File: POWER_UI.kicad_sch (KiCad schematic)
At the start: 45 parts, among them J601 PWR_IN1, J602 PWR_IN2, J603 PWR_IN3, J604 PWR_IN4, J605 MCP_INT, J606 5V, J607 GND, J608 3V3, J609 EX_PA, J610 EX_PB, J611 PWR_OUT1, J612 PWR_OUT3, J613 PWR_OUT2, J614 PWR_OUT4, Q601 IRLML9301TRPBF, Q602 IRLML9301TRPBF, Q603 IRLML9301TRPBF, Q604 IRLML9301TRPBF, U601 TLP291-4, U602 TLP291-4, U603 MCP23017_SS

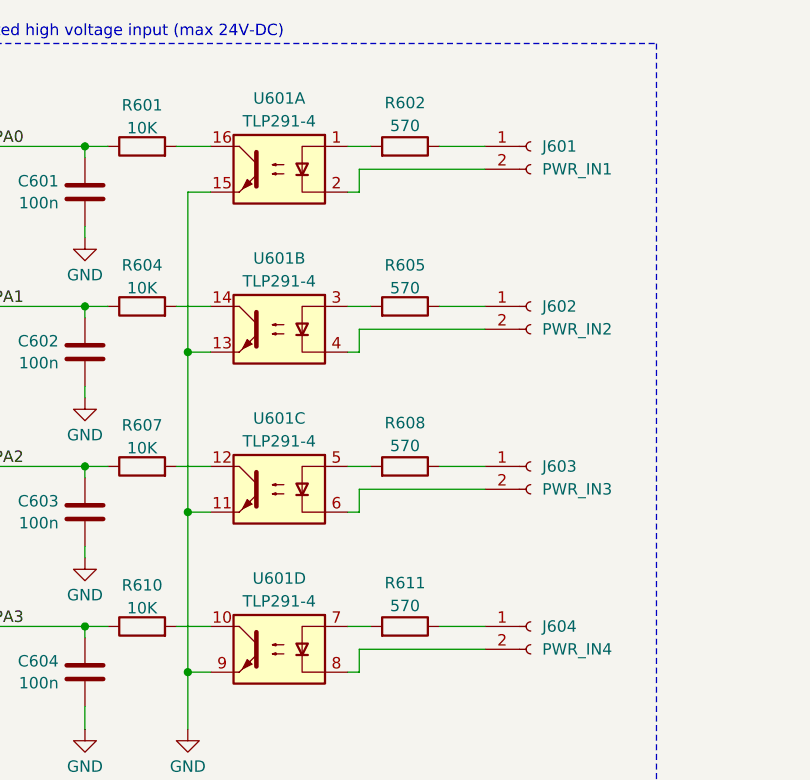
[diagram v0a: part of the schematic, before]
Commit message: added some lcsc PN, and uniformed some resistors values to reduce BOM count
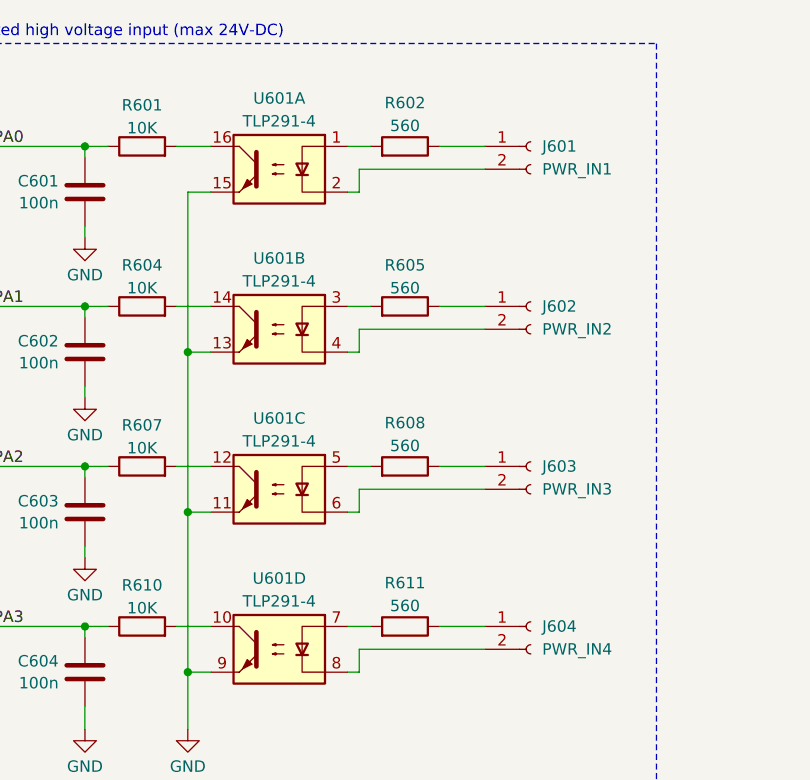
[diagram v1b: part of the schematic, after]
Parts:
- R602, R605, R608, R611: value 570 -> 560; LCSC (none) -> C23204
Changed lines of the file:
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@@
 			)
 		)
-		(property "Value" "570"
+		(property "Value" "560"
 			(at 165.1 30.734 90)
 			(effects
@@
 		)
 		(property "Sim.Type" ""
+			(at 165.1 33.02 90)
+			(effects
+				(font
+					(size 1.27 1.27)
+				)
+				(hide yes)
+			)
+		)
+		(property "LCSC" "C23204"
 			(at 165.1 33.02 90)
 			(effects
@@
 			)
 		)
-		(property "Value" "570"
+		(property "Value" "560"
 			(at 165.1 84.074 90)
 			(effects
@@
 		)
 		(property "Sim.Type" ""
+			(at 165.1 86.36 90)
+			(effects
+				(font
+					(size 1.27 1.27)
+				)
+				(hide yes)
+			)
+		)
+		(property "LCSC" "C23204"
 			(at 165.1 86.36 90)
 			(effects
@@
 			)
 		)
-		(property "Value" "570"
+		(property "Value" "560"
 			(at 165.1 66.294 90)
 			(effects
@@
 		)
 		(property "Sim.Type" ""
+			(at 165.1 68.58 90)
+			(effects
+				(font
+					(size 1.27 1.27)
+				)
+				(hide yes)
+			)
+		)
+		(property "LCSC" "C23204"
 			(at 165.1 68.58 90)
 			(effects
@@
 			)
 		)
-		(property "Value" "570"
+		(property "Value" "560"
 			(at 165.1 48.768 90)
 			(effects
@@
 			(at 165.1 50.8 90)
 			(effects
+				(font
+					(size 1.27 1.27)
+				)
+				(hide yes)
+			)
+		)
+		(property "LCSC" "C23204"
+			(at 165.1 50.8 90)
+			(effects

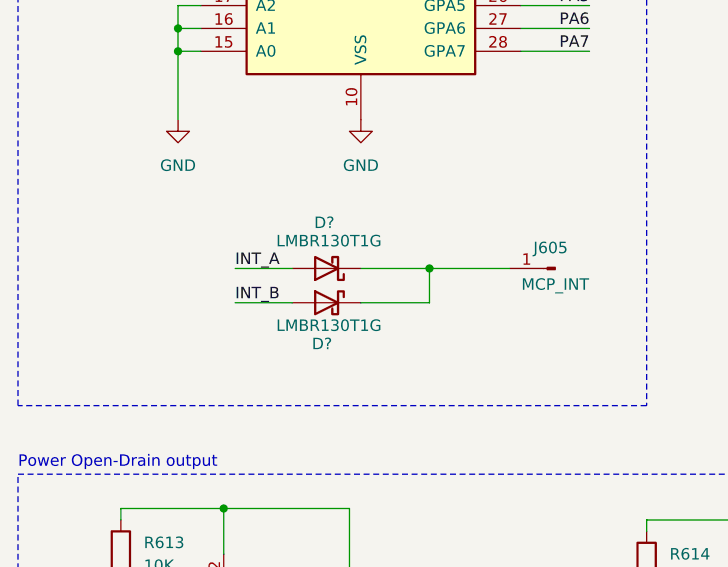
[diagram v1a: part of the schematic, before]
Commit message: Created buzzer footprint, and fixed some libraries simbols and footprint
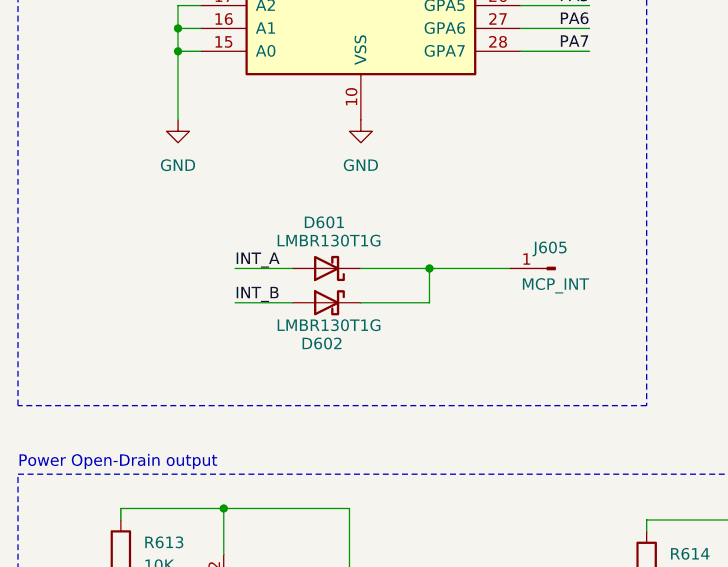
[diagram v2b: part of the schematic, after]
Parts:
- gave numbers to parts that had none: 2
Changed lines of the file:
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@@
 		(on_board yes)
 		(dnp no)
-		(property "Reference" "D?"
+		(property "Reference" "D602"
 			(at 59.182 109.982 0)
 			(effects
@@
 			(project "Educational-Board_MainBoard"
 				(path "/835b4df9-7d62-45f4-81d2-5a64fbc86f3c/ba7e13a3-22c7-43a3-af0e-4fb3e1cec0f6"
-					(reference "D?")
+					(reference "D602")
 					(unit 1)
 				)
@@
 		(on_board yes)
 		(dnp no)
-		(property "Reference" "D?"
+		(property "Reference" "D601"
 			(at 59.436 96.52 0)
 			(effects
@@
 			(project "Educational-Board_MainBoard"
 				(path "/835b4df9-7d62-45f4-81d2-5a64fbc86f3c/ba7e13a3-22c7-43a3-af0e-4fb3e1cec0f6"
-					(reference "D?")
-					(unit 1)
-				)
+					(reference "D601")
+					(unit 1)
+				)

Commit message: Started the checking of the components
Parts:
- C601, C602, C603, C604, D601, D602, J601, J602, J603, J604, J605, J606, J607, J608, J609, J610, J611, J612, J613, J614, JP601, JP602, Q601, Q602, Q603, Q604, R601, R602, R603, R604, R605, R606, R607, R608, R609, R610, R611, R612, R613, R614, R615, R616, U603: Checked (none) -> OK
- U601, U602: footprint Package_SO:SOIC-16_4.55x10.3mm_P1.27mm -> (none); Checked (none) -> Footprint

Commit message: Continued to check components footprints
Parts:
- U601, U602: Checked Footprint -> E- Footprint
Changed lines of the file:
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@@
 			)
 		)
-		(property "Checked" "Footprint"
+		(property "Checked" "E- Footprint"
 			(at 151.13 53.34 0)
 			(effects
@@
 			)
 		)
-		(property "Checked" "Footprint"
+		(property "Checked" "E- Footprint"
 			(at 242.57 71.12 0)
 			(effects
@@
 			)
 		)
-		(property "Checked" "Footprint"
+		(property "Checked" "E- Footprint"
 			(at 151.13 35.56 0)
 			(effects
@@
 			)
 		)
-		(property "Checked" "Footprint"
+		(property "Checked" "E- Footprint"
 			(at 242.57 35.56 0)
 			(effects
@@
 			)
 		)
-		(property "Checked" "Footprint"
+		(property "Checked" "E- Footprint"
 			(at 242.57 53.34 0)
 			(effects
@@
 			)
 		)
-		(property "Checked" "Footprint"
+		(property "Checked" "E- Footprint"
 			(at 151.13 88.9 0)
 			(effects
@@
 			)
 		)
-		(property "Checked" "Footprint"
+		(property "Checked" "E- Footprint"
 			(at 151.13 71.12 0)
 			(effects
@@
 			)
 		)
-		(property "Checked" "Footprint"
+		(property "Checked" "E- Footprint"
 			(at 242.57 88.9 0)
 			(effects

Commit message: Continued the floor plan
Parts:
- U601, U602: footprint (none) -> Package_SO:SOP-16_4.4x10.4mm_P1.27mm; Checked E- Footprint -> OK
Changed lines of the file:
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@@
 			)
 		)
-		(property "Footprint" ""
+		(property "Footprint" "Package_SO:SOP-16_4.4x10.4mm_P1.27mm"
 			(at 156.21 58.42 0)
 			(effects
@@
 			)
 		)
-		(property "Checked" "E- Footprint"
+		(property "Checked" "OK"
 			(at 151.13 53.34 0)
 			(effects
@@
 			)
 		)
-		(property "Footprint" ""
+		(property "Footprint" "Package_SO:SOP-16_4.4x10.4mm_P1.27mm"
 			(at 237.49 76.2 0)
 			(effects
@@
 			)
 		)
-		(property "Checked" "E- Footprint"
+		(property "Checked" "OK"
 			(at 242.57 71.12 0)
 			(effects
@@
 			)
 		)
-		(property "Footprint" ""
+		(property "Footprint" "Package_SO:SOP-16_4.4x10.4mm_P1.27mm"
 			(at 156.21 40.64 0)
 			(effects
@@
 			)
 		)
-		(property "Checked" "E- Footprint"
+		(property "Checked" "OK"
 			(at 151.13 35.56 0)
 			(effects
@@
 			)
 		)
-		(property "Footprint" ""
+		(property "Footprint" "Package_SO:SOP-16_4.4x10.4mm_P1.27mm"
 			(at 237.49 40.64 0)
 			(effects
@@
 			)
 		)
-		(property "Checked" "E- Footprint"
+		(property "Checked" "OK"
 			(at 242.57 35.56 0)
 			(effects
@@
 			)
 		)
-		(property "Footprint" ""
+		(property "Footprint" "Package_SO:SOP-16_4.4x10.4mm_P1.27mm"
 			(at 237.49 58.42 0)
 			(effects
@@
 			)
 		)
-		(property "Checked" "E- Footprint"
+		(property "Checked" "OK"
 			(at 242.57 53.34 0)
 			(effects
@@
 			)
 		)
-		(property "Footprint" ""
+		(property "Footprint" "Package_SO:SOP-16_4.4x10.4mm_P1.27mm"
 			(at 156.21 93.98 0)
 			(effects
@@
 			)
 		)
-		(property "Checked" "E- Footprint"
+		(property "Checked" "OK"
 			(at 151.13 88.9 0)
 			(effects
@@
 			)
 		)
-		(property "Footprint" ""
+		(property "Footprint" "Package_SO:SOP-16_4.4x10.4mm_P1.27mm"
 			(at 156.21 76.2 0)
 			(effects
@@
 			)
 		)
-		(property "Checked" "E- Footprint"
+		(property "Checked" "OK"
 			(at 151.13 71.12 0)
 			(effects
@@
 			)
 		)
-		(property "Footprint" ""
+		(property "Footprint" "Package_SO:SOP-16_4.4x10.4mm_P1.27mm"
 			(at 237.49 93.98 0)
 			(effects
@@
 			)
 		)
-		(property "Checked" "E- Footprint"
+		(property "Checked" "OK"
 			(at 242.57 88.9 0)
 			(effects

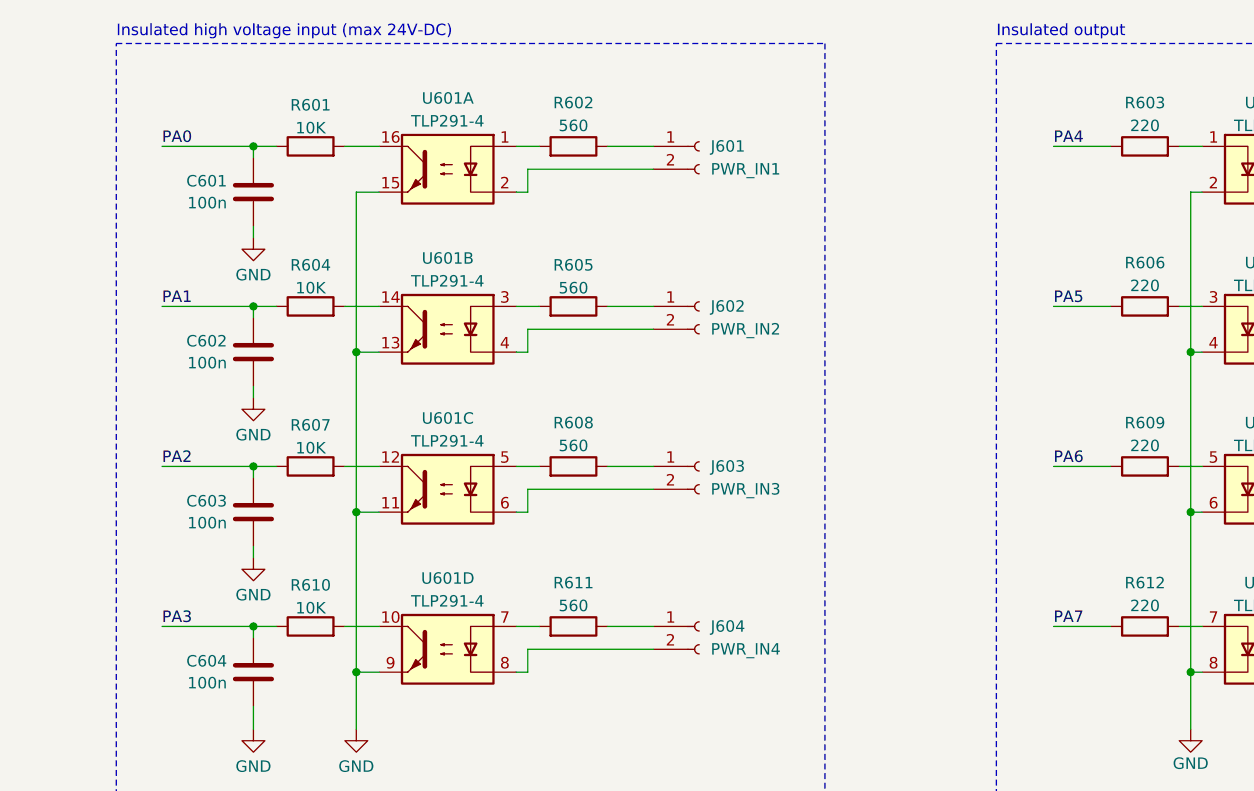
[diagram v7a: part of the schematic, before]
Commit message: Roued the majority of the nets of the POWER IO
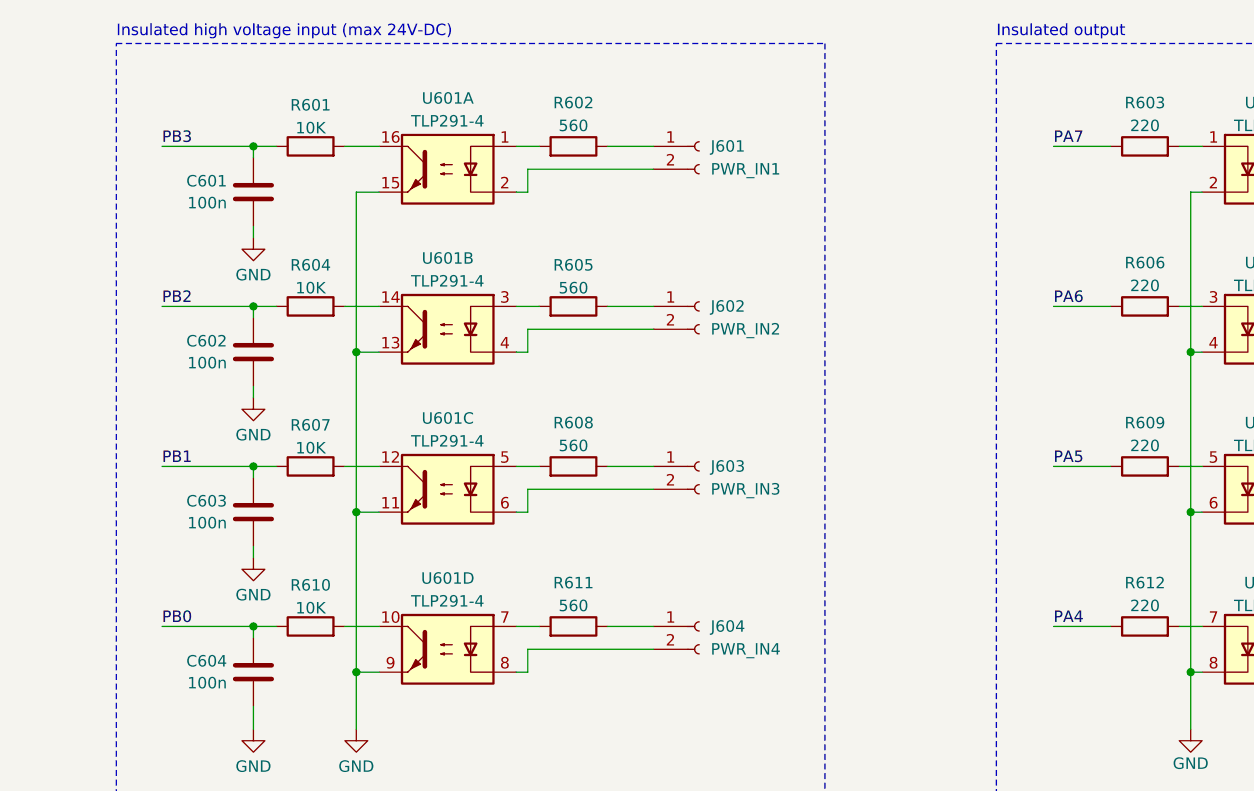
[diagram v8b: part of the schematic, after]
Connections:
- net PA0: no longer C601.1, R601.1
- net PA1: no longer C602.1, R604.1
- net PA2: no longer C603.1, R607.1
- net PA3: no longer C604.1, R610.1
- net PA4: now also R612.1; no longer R603.1
- net PA5: now also R609.1; no longer R606.1
- net PA6: now also R606.1; no longer R609.1
- net PA7: now also R603.1; no longer R612.1
- net PB0: now also C604.1, R610.1
- net PB1: now also C603.1, R607.1
- net PB2: now also C602.1, R604.1
- net PB3: now also C601.1, R601.1
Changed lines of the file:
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@@
 		)
 	)
-	(label "PA6"
+	(label "PA5"
 		(at 218.44 68.58 0)
 		(effects
@@
 		)
 	)
-	(label "PA0"
+	(label "PB3"
 		(at 119.38 33.02 0)
 		(effects
@@
 		)
 	)
-	(label "PA7"
+	(label "PA4"
 		(at 218.44 86.36 0)
 		(effects
@@
 		)
 	)
-	(label "PA4"
+	(label "PA7"
 		(at 218.44 33.02 0)
 		(effects
@@
 		)
 	)
-	(label "PA1"
+	(label "PB2"
 		(at 119.38 50.8 0)
 		(effects
@@
 		)
 	)
-	(label "PA5"
+	(label "PA6"
 		(at 218.44 50.8 0)
 		(effects
@@
 		)
 	)
-	(label "PA3"
+	(label "PB0"
 		(at 119.38 86.36 0)
 		(effects
@@
 		)
 	)
-	(label "PA2"
+	(label "PB1"
 		(at 119.38 68.58 0)
 		(effects
@@
 		(length 2.54)
 		(shape round)
-		(at 109.22 180.34 180)
-		(effects
-			(font
-				(size 1.27 1.27)
-			)
-			(justify right bottom)
-		)
-		(property "Netclass" "Power"
-			(at 110.49 182.88 0)
-			(effects
-				(font
-					(size 1.27 1.27)
-				)
-				(justify left)
-				(hide yes)
-			)
-		)
-		(property "Component Class" ""
-			(at -106.68 129.54 0)
-			(effects
-				(font
-					(size 1.27 1.27)
-					(italic yes)
-				)
-			)
-		)
-	)
-	(netclass_flag ""
-		(length 2.54)
-		(shape round)
-		(at 50.8 180.34 180)
-		(effects
-			(font
-				(size 1.27 1.27)
-			)
-			(justify right bottom)
-		)
-		(property "Netclass" "Power"
-			(at 52.07 182.88 0)
-			(effects
-				(font
-					(size 1.27 1.27)
-				)
-				(justify left)
-				(hide yes)
-			)
-		)
-		(property "Component Class" ""
-			(at -165.1 129.54 0)
-			(effects
-				(font
-					(size 1.27 1.27)
-					(italic yes)
-				)
-			)
-		)
-	)
-	(netclass_flag ""
-		(length 2.54)
-		(shape round)
 		(at 171.45 88.9 180)
 		(fields_autoplaced yes)
@@
 		(length 2.54)
 		(shape round)
-		(at 109.22 148.59 180)
-		(effects
-			(font
-				(size 1.27 1.27)
-			)
-			(justify right bottom)
-		)
-		(property "Netclass" "Power"
-			(at 110.49 151.13 0)
-			(effects
-				(font
-					(size 1.27 1.27)
-				)
-				(justify left)
-				(hide yes)
-			)
-		)
-		(property "Component Class" ""
-			(at -106.68 97.79 0)
-			(effects
-				(font
-					(size 1.27 1.27)
-					(italic yes)
-				)
-			)
-		)
-	)
-	(netclass_flag ""
-		(length 2.54)
-		(shape round)
 		(at 160.02 50.8 0)
 		(effects
@@
 			(effects
 				(font
-					(size 1.27 1.27)
-					(italic yes)
-				)
-			)
-		)
-	)
-	(netclass_flag ""
-		(length 2.54)
-		(shape round)
-		(at 50.8 147.32 180)
-		(effects
-			(font
-				(size 1.27 1.27)
-			)
-			(justify right bottom)
-		)
-		(property "Netclass" "Power"
-			(at 52.07 149.86 0)
-			(effects
-				(font
-					(size 1.27 1.27)
-				)
-				(justify left)
-				(hide yes)
-			)
-		)
-		(property "Component Class" ""
-			(at -165.1 96.52 0)
-			(effects
-				(font
